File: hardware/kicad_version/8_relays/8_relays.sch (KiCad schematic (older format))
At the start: 78 parts, among them K101 CONN_3, K102 J_IN, K103 CONN_3, K104 J_OUT, K105 G5LA-1-12VDC, K106 G5LA-1-12VDC, K107 G5LA-1-12VDC, K108 G5LA-1-12VDC, K109 G5LA-1-12VDC, K110 G5LA-1-12VDC, K111 G5LA-1-12VDC, K112 G5LA-1-12VDC, K113 CONN_3, K114 CONN_3, K115 CONN_3, K116 CONN_3, K117 CONN_3, K118 CONN_3, K119 CONN_3, K120 CONN_3, Q101 DSS20201L NPN, Q102 DSS20201L NPN, Q103 DSS20201L NPN, Q104 DSS20201L NPN, Q105 DSS20201L NPN, Q106 DSS20201L NPN, Q107 DSS20201L NPN, Q108 DSS20201L NPN, Q109 NPN, Q110 NPN, Q111 NPN, Q112 NPN, Q113 NPN, Q114 NPN, Q115 NPN, Q116 NPN, U101 74HC595

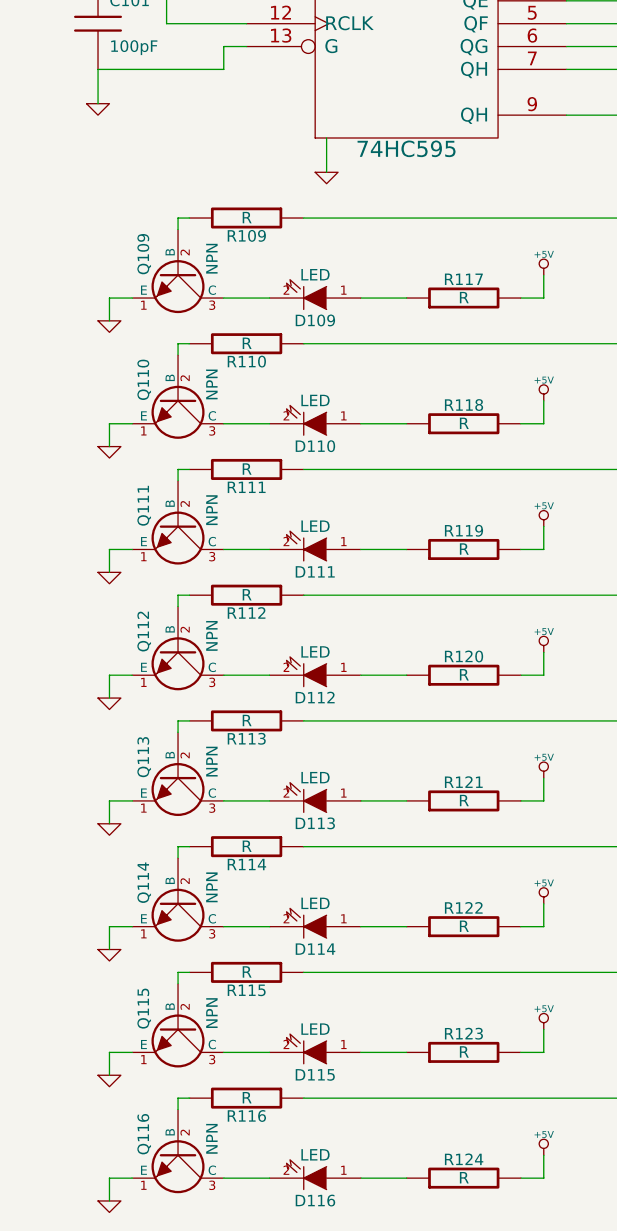
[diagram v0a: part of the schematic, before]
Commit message: Added relay footprint and NPN reference
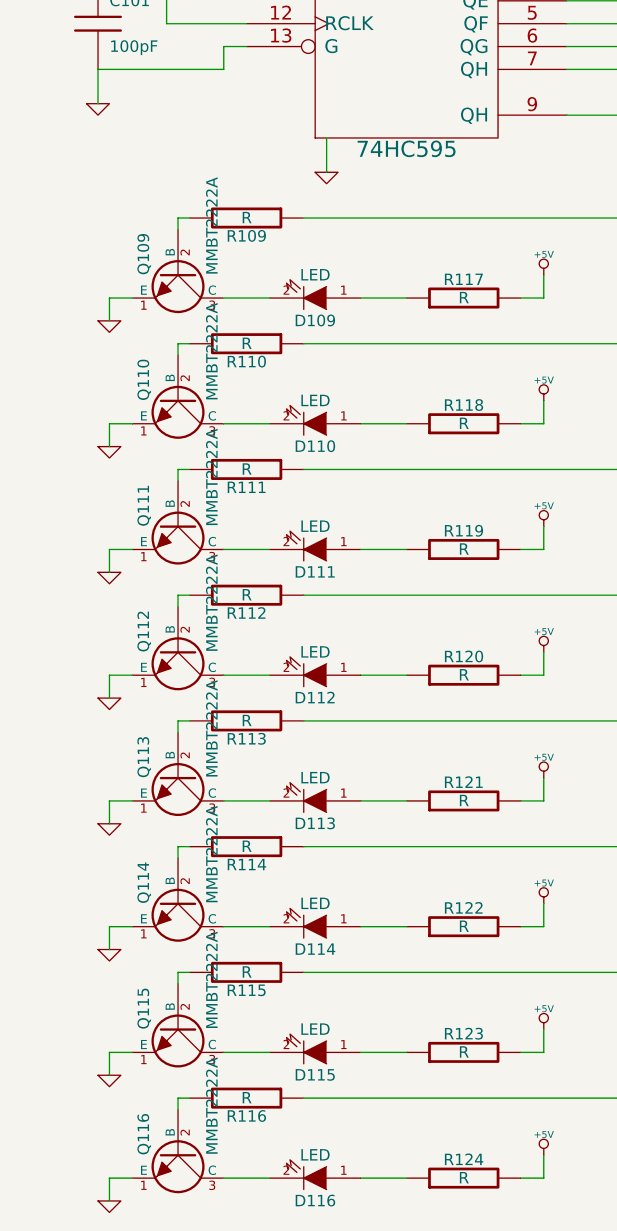
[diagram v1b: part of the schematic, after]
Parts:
- Q109, Q110, Q111, Q112, Q113, Q114, Q115, Q116: value NPN -> MMBT2222A
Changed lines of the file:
@@
-EESchema Schematic File Version 2  date 01/04/2012 09:49:35
+EESchema Schematic File Version 2  date 01/04/2012 14:12:18
 LIBS:power
 LIBS:device
@@
 $EndComp
 $Comp
-L +5V #PWR116
+L +5V #PWR01
 U 1 1 4F780535
 P 2950 3350
-F 0 "#PWR116" H 2950 3440 20  0001 C CNN
+F 0 "#PWR01" H 2950 3440 20  0001 C CNN
 F 1 "+5V" H 2950 3440 30  0000 C CNN
 	1    2950 3350
@@
 $EndComp
 $Comp
-L GND #PWR103
+L GND #PWR02
 U 1 1 4F780534
 P 1050 3550
-F 0 "#PWR103" H 1050 3550 30  0001 C CNN
+F 0 "#PWR02" H 1050 3550 30  0001 C CNN
 F 1 "GND" H 1050 3480 30  0001 C CNN
 	1    1050 3550
@@
 P 1350 3350
 F 0 "Q109" H 1350 3200 50  0000 R CNN
-F 1 "NPN" H 1350 3500 50  0000 R CNN
+F 1 "MMBT2222A" H 1350 3500 50  0000 R CNN
 	1    1350 3350
 	0    1    1    0
@@
 P 1350 3900
 F 0 "Q110" H 1350 3750 50  0000 R CNN
-F 1 "NPN" H 1350 4050 50  0000 R CNN
+F 1 "MMBT2222A" H 1350 4050 50  0000 R CNN
 	1    1350 3900
 	0    1    1    0
@@
 $EndComp
 $Comp
-L GND #PWR104
+L GND #PWR03
 U 1 1 4F78052D
 P 1050 4100
-F 0 "#PWR104" H 1050 4100 30  0001 C CNN
+F 0 "#PWR03" H 1050 4100 30  0001 C CNN
 F 1 "GND" H 1050 4030 30  0001 C CNN
 	1    1050 4100
@@
 $EndComp
 $Comp
-L +5V #PWR117
+L +5V #PWR04
 U 1 1 4F78052C
 P 2950 3900
-F 0 "#PWR117" H 2950 3990 20  0001 C CNN
+F 0 "#PWR04" H 2950 3990 20  0001 C CNN
 F 1 "+5V" H 2950 3990 30  0000 C CNN
 	1    2950 3900
@@
 P 1350 5550
 F 0 "Q113" H 1350 5400 50  0000 R CNN
-F 1 "NPN" H 1350 5700 50  0000 R CNN
+F 1 "MMBT2222A" H 1350 5700 50  0000 R CNN
 	1    1350 5550
 	0    1    1    0
@@
 $EndComp
 $Comp
-L GND #PWR107
+L GND #PWR05
 U 1 1 4F780527
 P 1050 5750
-F 0 "#PWR107" H 1050 5750 30  0001 C CNN
+F 0 "#PWR05" H 1050 5750 30  0001 C CNN
 F 1 "GND" H 1050 5680 30  0001 C CNN
 	1    1050 5750
@@
 $EndComp
 $Comp
-L +5V #PWR120
+L +5V #PWR06
 U 1 1 4F780526
 P 2950 5550
-F 0 "#PWR120" H 2950 5640 20  0001 C CNN
+F 0 "#PWR06" H 2950 5640 20  0001 C CNN
 F 1 "+5V" H 2950 5640 30  0000 C CNN
 	1    2950 5550
@@
 $EndComp
 $Comp
-L +5V #PWR119
+L +5V #PWR07
 U 1 1 4F780523
 P 2950 5000
-F 0 "#PWR119" H 2950 5090 20  0001 C CNN
+F 0 "#PWR07" H 2950 5090 20  0001 C CNN
 F 1 "+5V" H 2950 5090 30  0000 C CNN
 	1    2950 5000
@@
 $EndComp
 $Comp
-L GND #PWR106
+L GND #PWR08
 U 1 1 4F780522
 P 1050 5200
-F 0 "#PWR106" H 1050 5200 30  0001 C CNN
+F 0 "#PWR08" H 1050 5200 30  0001 C CNN
 F 1 "GND" H 1050 5130 30  0001 C CNN
 	1    1050 5200
@@
 P 1350 5000
 F 0 "Q112" H 1350 4850 50  0000 R CNN
-F 1 "NPN" H 1350 5150 50  0000 R CNN
+F 1 "MMBT2222A" H 1350 5150 50  0000 R CNN
 	1    1350 5000
 	0    1    1    0
@@
 P 1350 4450
 F 0 "Q111" H 1350 4300 50  0000 R CNN
-F 1 "NPN" H 1350 4600 50  0000 R CNN
+F 1 "MMBT2222A" H 1350 4600 50  0000 R CNN
 	1    1350 4450
 	0    1    1    0
@@
 $EndComp
 $Comp
-L GND #PWR105
+L GND #PWR09
 U 1 1 4F78051B
 P 1050 4650
-F 0 "#PWR105" H 1050 4650 30  0001 C CNN
+F 0 "#PWR09" H 1050 4650 30  0001 C CNN
 F 1 "GND" H 1050 4580 30  0001 C CNN
 	1    1050 4650
@@
 $EndComp
 $Comp
-L +5V #PWR118
+L +5V #PWR010
 U 1 1 4F78051A
 P 2950 4450
-F 0 "#PWR118" H 2950 4540 20  0001 C CNN
+F 0 "#PWR010" H 2950 4540 20  0001 C CNN
 F 1 "+5V" H 2950 4540 30  0000 C CNN
 	1    2950 4450
@@
 $EndComp
 $Comp
-L +5V #PWR121
+L +5V #PWR011
 U 1 1 4F780510
 P 2950 6100
-F 0 "#PWR121" H 2950 6190 20  0001 C CNN
+F 0 "#PWR011" H 2950 6190 20  0001 C CNN
 F 1 "+5V" H 2950 6190 30  0000 C CNN
 	1    2950 6100
@@
 $EndComp
 $Comp
-L GND #PWR108
+L GND #PWR012
 U 1 1 4F78050F
 P 1050 6300
-F 0 "#PWR108" H 1050 6300 30  0001 C CNN
+F 0 "#PWR012" H 1050 6300 30  0001 C CNN
 F 1 "GND" H 1050 6230 30  0001 C CNN
 	1    1050 6300
@@
 P 1350 6100
 F 0 "Q114" H 1350 5950 50  0000 R CNN
-F 1 "NPN" H 1350 6250 50  0000 R CNN
+F 1 "MMBT2222A" H 1350 6250 50  0000 R CNN
 	1    1350 6100
 	0    1    1    0
@@
 P 1350 6650
 F 0 "Q115" H 1350 6500 50  0000 R CNN
-F 1 "NPN" H 1350 6800 50  0000 R CNN
+F 1 "MMBT2222A" H 1350 6800 50  0000 R CNN
 	1    1350 6650
 	0    1    1    0
@@
 $EndComp
 $Comp
-L GND #PWR109
+L GND #PWR013
 U 1 1 4F780500
 P 1050 6850
-F 0 "#PWR109" H 1050 6850 30  0001 C CNN
+F 0 "#PWR013" H 1050 6850 30  0001 C CNN
 F 1 "GND" H 1050 6780 30  0001 C CNN
 	1    1050 6850
@@
 $EndComp
 $Comp
-L +5V #PWR122
+L +5V #PWR014
 U 1 1 4F7804FF
 P 2950 6650
-F 0 "#PWR122" H 2950 6740 20  0001 C CNN
+F 0 "#PWR014" H 2950 6740 20  0001 C CNN
 F 1 "+5V" H 2950 6740 30  0000 C CNN
 	1    2950 6650
@@
 $EndComp
 $Comp
-L +5V #PWR123
+L +5V #PWR015
 U 1 1 4F7804A3
 P 2950 7200
-F 0 "#PWR123" H 2950 7290 20  0001 C CNN
+F 0 "#PWR015" H 2950 7290 20  0001 C CNN
 F 1 "+5V" H 2950 7290 30  0000 C CNN
 	1    2950 7200
@@
 $EndComp
 $Comp
-L GND #PWR110
+L GND #PWR016
 U 1 1 4F780490
 P 1050 7400
-F 0 "#PWR110" H 1050 7400 30  0001 C CNN
+F 0 "#PWR016" H 1050 7400 30  0001 C CNN
 F 1 "GND" H 1050 7330 30  0001 C CNN
 	1    1050 7400
@@
 P 1350 7200
 F 0 "Q116" H 1350 7050 50  0000 R CNN
-F 1 "NPN" H 1350 7350 50  0000 R CNN
+F 1 "MMBT2222A" H 1350 7350 50  0000 R CNN
 	1    1350 7200
 	0    1    1    0
 $EndComp
 $Comp
-L GND #PWR127
+L GND #PWR017
 U 1 1 4F63A4E0
 P 5300 1800
-F 0 "#PWR127" H 5300 1800 30  0001 C CNN
+F 0 "#PWR017" H 5300 1800 30  0001 C CNN
 F 1 "GND" H 5300 1730 30  0001 C CNN
 	1    5300 1800
@@
 $EndComp
 $Comp
-L GND #PWR128
+L GND #PWR018
 U 1 1 4F63A4DC
 P 5700 2450
-F 0 "#PWR128" H 5700 2450 30  0001 C CNN
+F 0 "#PWR018" H 5700 2450 30  0001 C CNN
 F 1 "GND" H 5700 2380 30  0001 C CNN
 	1    5700 2450
@@
 $EndComp
 $Comp
-L GND #PWR129
+L GND #PWR019
 U 1 1 4F63A454
 P 6100 3100
-F 0 "#PWR129" H 6100 3100 30  0001 C CNN
+F 0 "#PWR019" H 6100 3100 30  0001 C CNN
 F 1 "GND" H 6100 3030 30  0001 C CNN
 	1    6100 3100
@@
 $EndComp
 $Comp
-L GND #PWR130
+L GND #PWR020
 U 1 1 4F63A32F
 P 6500 3750
-F 0 "#PWR130" H 6500 3750 30  0001 C CNN
+F 0 "#PWR020" H 6500 3750 30  0001 C CNN
 F 1 "GND" H 6500 3680 30  0001 C CNN
 	1    6500 3750
@@
 $EndComp
 $Comp
-L +12V #PWR135
+L +12V #PWR021
 U 1 1 4F63A241
 P 8450 1150
-F 0 "#PWR135" H 8450 1100 20  0001 C CNN
+F 0 "#PWR021" H 8450 1100 20  0001 C CNN
 F 1 "+12V" H 8450 1250 30  0000 C CNN
 	1    8450 1150
@@
 $EndComp
 $Comp
-L GND #PWR131
+L GND #PWR022
 U 1 1 4F639213
 P 6900 4400
-F 0 "#PWR131" H 6900 4400 30  0001 C CNN
+F 0 "#PWR022" H 6900 4400 30  0001 C CNN
 F 1 "GND" H 6900 4330 30  0001 C CNN
 	1    6900 4400
@@
 $EndComp
 $Comp
-L GND #PWR132
+L GND #PWR023
 U 1 1 4F63920F
 P 7300 5050
-F 0 "#PWR132" H 7300 5050 30  0001 C CNN
+F 0 "#PWR023" H 7300 5050 30  0001 C CNN
 F 1 "GND" H 7300 4980 30  0001 C CNN
 	1    7300 5050
@@
 $EndComp
 $Comp
-L GND #PWR133
+L GND #PWR024
 U 1 1 4F63920A
 P 7700 5700
-F 0 "#PWR133" H 7700 5700 30  0001 C CNN
+F 0 "#PWR024" H 7700 5700 30  0001 C CNN
 F 1 "GND" H 7700 5630 30  0001 C CNN
 	1    7700 5700
@@
 $EndComp
 $Comp
-L GND #PWR134
+L GND #PWR025
 U 1 1 4F639205
 P 8100 6350
-F 0 "#PWR134" H 8100 6350 30  0001 C CNN
+F 0 "#PWR025" H 8100 6350 30  0001 C CNN
 F 1 "GND" H 8100 6280 30  0001 C CNN
 	1    8100 6350
@@
 $EndComp
 $Comp
-L GND #PWR113
+L GND #PWR026
 U 1 1 4F455D3D
 P 1450 800
-F 0 "#PWR113" H 1450 800 30  0001 C CNN
+F 0 "#PWR026" H 1450 800 30  0001 C CNN
 F 1 "GND" H 1450 730 30  0001 C CNN
 	1    1450 800
@@
 $EndComp
 $Comp
-L +12V #PWR111
+L +12V #PWR027
 U 1 1 4F455D2D
 P 1250 650
-F 0 "#PWR111" H 1250 600 20  0001 C CNN
+F 0 "#PWR027" H 1250 600 20  0001 C CNN
 F 1 "+12V" H 1250 750 30  0000 C CNN
 	1    1250 650
@@
 $EndComp
 $Comp
-L +5V #PWR112
+L +5V #PWR028
 U 1 1 4F455D19
 P 1250 850
-F 0 "#PWR112" H 1250 940 20  0001 C CNN
+F 0 "#PWR028" H 1250 940 20  0001 C CNN
 F 1 "+5V" H 1250 940 30  0000 C CNN
 	1    1250 850
@@
 $EndComp
 $Comp
-L +12V #PWR125
+L +12V #PWR029
 U 1 1 4F455CF3
 P 3450 650
-F 0 "#PWR125" H 3450 600 20  0001 C CNN
+F 0 "#PWR029" H 3450 600 20  0001 C CNN
 F 1 "+12V" H 3450 750 30  0000 C CNN
 	1    3450 650
@@
 $EndComp
 $Comp
-L GND #PWR124
+L GND #PWR030
 U 1 1 4F455CDC
 P 3200 800
-F 0 "#PWR124" H 3200 800 30  0001 C CNN
+F 0 "#PWR030" H 3200 800 30  0001 C CNN
 F 1 "GND" H 3200 730 30  0001 C CNN
 	1    3200 800
@@
 $EndComp
 $Comp
-L +5V #PWR126
+L +5V #PWR031
 U 1 1 4F455CA2
 P 3450 850
-F 0 "#PWR126" H 3450 940 20  0001 C CNN
+F 0 "#PWR031" H 3450 940 20  0001 C CNN
 F 1 "+5V" H 3450 940 30  0000 C CNN
 	1    3450 850
@@
 $EndComp
 $Comp
-L +5V #PWR114
+L +5V #PWR032
 U 1 1 4F455A3A
 P 2000 1550
-F 0 "#PWR114" H 2000 1640 20  0001 C CNN
+F 0 "#PWR032" H 2000 1640 20  0001 C CNN
 F 1 "+5V" H 2000 1640 30  0000 C CNN
 	1    2000 1550
@@
 $EndComp
 $Comp
-L GND #PWR115
+L GND #PWR033
 U 1 1 4F4559F6
 P 2000 2900
-F 0 "#PWR115" H 2000 2900 30  0001 C CNN
+F 0 "#PWR033" H 2000 2900 30  0001 C CNN
 F 1 "GND" H 2000 2830 30  0001 C CNN
 	1    2000 2900
@@
 $EndComp
 $Comp
-L GND #PWR102
+L GND #PWR034
 U 1 1 4F4559E7
 P 1000 2600
-F 0 "#PWR102" H 1000 2600 30  0001 C CNN
+F 0 "#PWR034" H 1000 2600 30  0001 C CNN
 F 1 "GND" H 1000 2530 30  0001 C CNN
 	1    1000 2600
@@
 $EndComp
 $Comp
-L +5V #PWR101
+L +5V #PWR035
 U 1 1 4F4559CC
 P 1000 1900
-F 0 "#PWR101" H 1000 1990 20  0001 C CNN
+F 0 "#PWR035" H 1000 1990 20  0001 C CNN
 F 1 "+5V" H 1000 1990 30  0000 C CNN
 	1    1000 1900
